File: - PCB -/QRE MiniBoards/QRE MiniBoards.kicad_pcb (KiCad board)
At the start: 2 copper layers, 90 x 11 mm, 7 parts, among them J2 Conn_01x04_Pin, U1 QRE1113, U2 QRE1113

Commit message: QRE MiniBoards - Finito
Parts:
- added H1: MountingHole, MountingHole:MountingHole_3.2mm_M3_ISO7380_Pad, F.Cu at (117.5, 68.0)
- added H2: MountingHole, MountingHole:MountingHole_3.2mm_M3_ISO7380_Pad, F.Cu at (157.5, 68.0)
- U1, U2: moved to B.Cu
- moved R4 6.36 mm to (174.9, 68.0)
- moved R3 6.35 mm to (181.1, 68.1), turned to 90 degrees
- moved U1 1.80 mm to (97.9, 68.0), turned to 180 degrees
- moved U2 1.80 mm to (178.9, 68.0), turned to 180 degrees
- moved R1 1.40 mm to (93.9, 68.0), turned to 90 degrees
- moved R2 1.40 mm to (100.1, 68.0)
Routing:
- net +3V3: track 15.0 -> 93.9 mm
- net Net-(U1-A): track 0.00 -> 4.66 mm
- net QRE1113 A: track 37.7 -> 41.9 mm
- net QRE1113 B: track 43.2 -> 40.9 mm
- net Net-(U2-A): track 2.24 -> 3.71 mm
- added copper zone on B.Cu, net GND
- added copper zone on F.Cu, net GND

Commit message: QRE MiniBoards
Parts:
- H1, H2: value MountingHole -> M3; footprint MountingHole:MountingHole_3.2mm_M3_ISO7380_Pad -> MountingHole:MountingHole_3.2mm_M3_Pad
- J2: footprint Connector_JST:JST_PH_B4B-PH-SM4-TB_1x04-1MP_P2.00mm_Vertical -> Connector_Molex:Molex_PicoBlade_53398-0471_1x04-1MP_P1.25mm_Vertical
- moved J2 2.45 mm to (137.5, 66.3)
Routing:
- net +3V3: track 93.9 -> 98.3 mm
- net QRE1113 A: track 41.9 -> 45.2 mm
- net QRE1113 B: track 40.9 -> 42.9 mm
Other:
- board text added: "W"

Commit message: QRE MiniBoards - update
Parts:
- J2: footprint Connector_Molex:Molex_PicoBlade_53398-0471_1x04-1MP_P1.25mm_Vertical -> Connector_Molex:Molex_PicoBlade_53261-0471_1x04-1MP_P1.25mm_Horizontal
- R1, R2, R3, R4: footprint Resistor_SMD:R_1206_3216Metric_Pad1.30x1.75mm_HandSolder -> Resistor_SMD:R_0805_2012Metric_Pad1.20x1.40mm_HandSolder
- U1, U2: footprint sumec_library:OnSemi_CASE100AQ - QRE1113 -> qre_miniboard_library:OnSemi_CASE100AQ - QRE1113
- moved R1 0.80 mm to (93.9, 67.2)
- moved R2 0.80 mm to (100.1, 67.2)
- moved R3 0.80 mm to (181.1, 67.2)
- moved R4 0.80 mm to (174.9, 67.2)
- moved J2 0.60 mm to (137.2, 65.8), turned to 180 degrees
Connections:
- J2 pad 1: QRE1113 A -> QRE1113 B
- J2 pad 4: QRE1113 B -> QRE1113 A
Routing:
- net +3V3: track 98.3 -> 96.2 mm, vias 0 -> 4
- net Net-(U1-A): track 4.66 -> 5.83 mm
- net Net-(U2-A): track 3.71 -> 4.78 mm
- net QRE1113 A: track 45.2 -> 44.2 mm
- net QRE1113 B: track 42.9 -> 43.8 mm

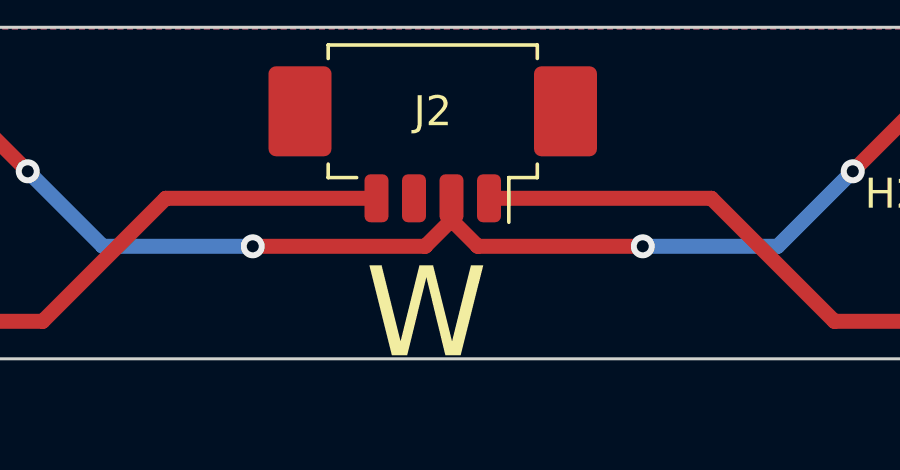
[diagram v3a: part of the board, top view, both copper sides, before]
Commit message: Updates:
GyroScope project file, QRE1113 Board update and BOM, SMDv2 iBOM and schematic update.
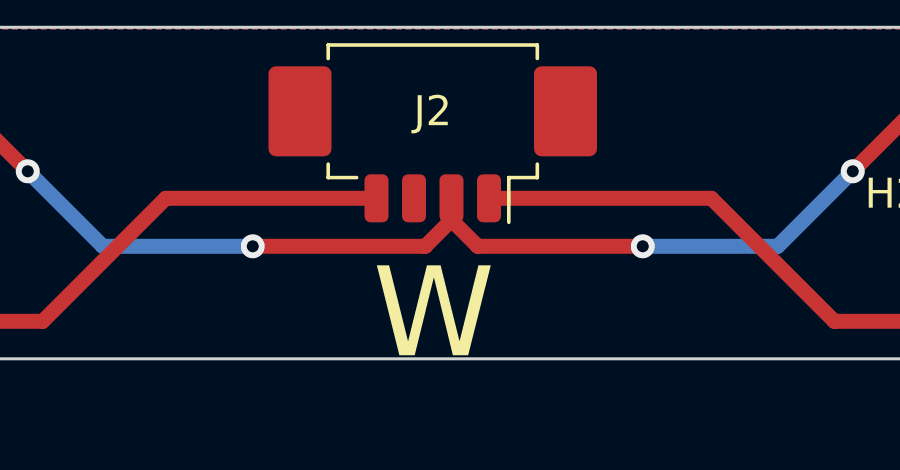
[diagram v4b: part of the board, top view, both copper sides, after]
